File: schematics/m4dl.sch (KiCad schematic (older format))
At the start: 71 parts

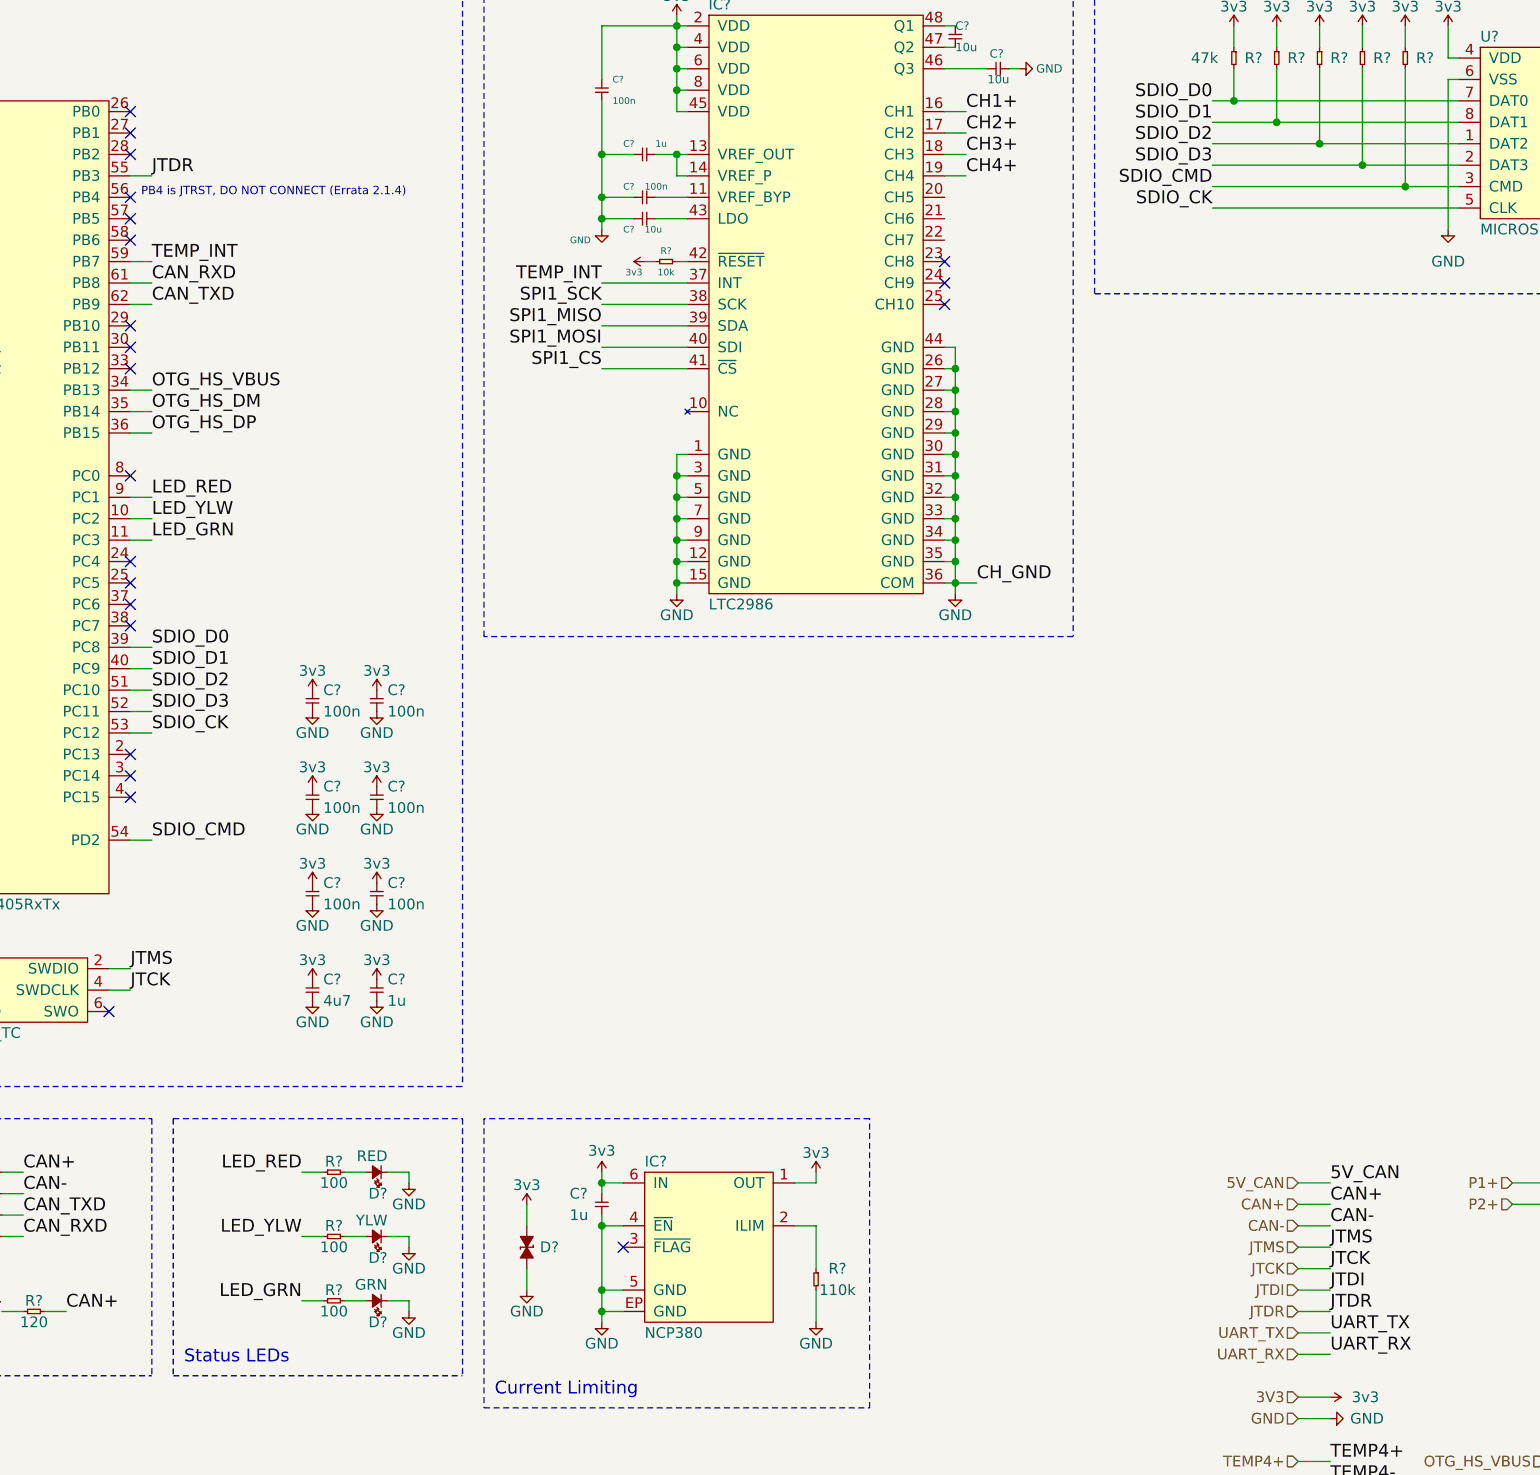
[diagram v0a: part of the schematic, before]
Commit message: Chain JTAG connections
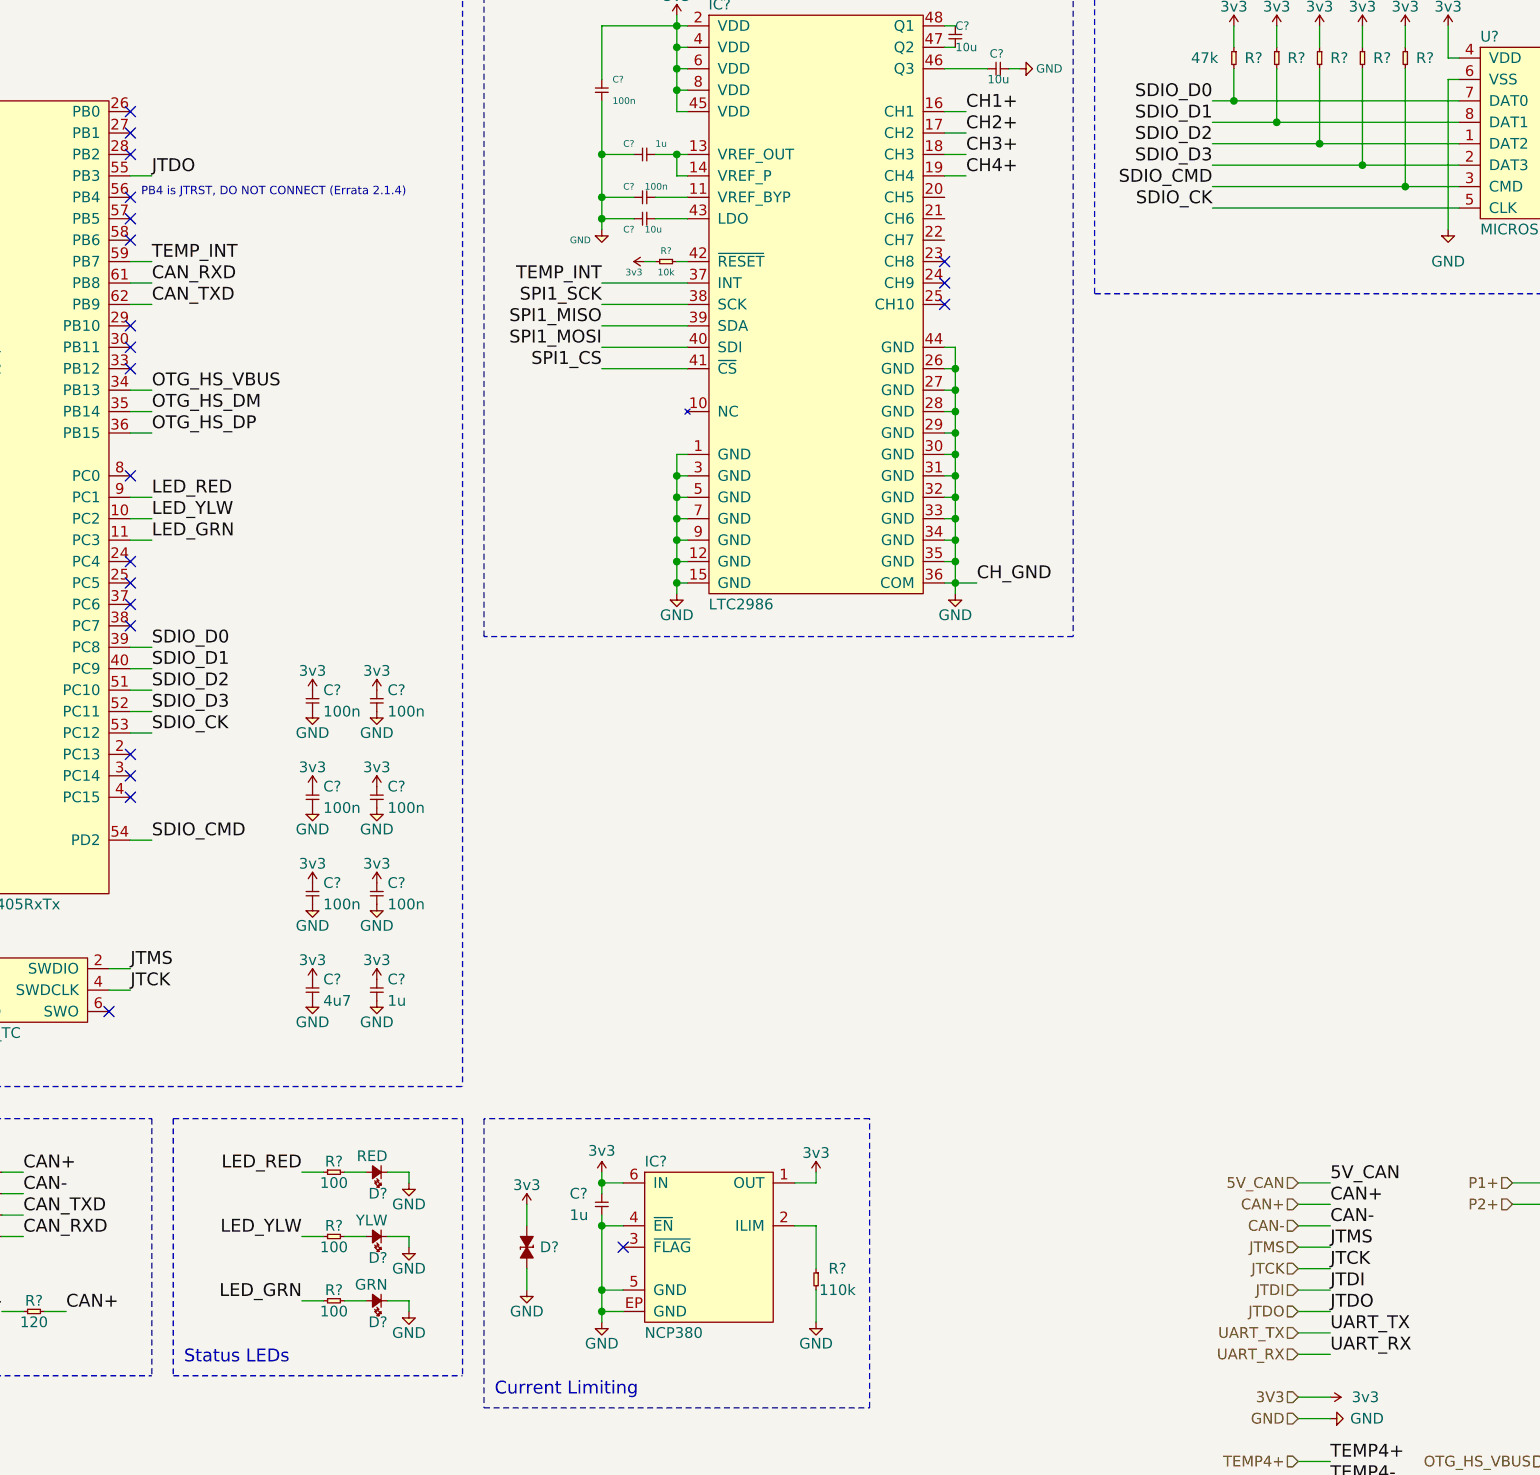
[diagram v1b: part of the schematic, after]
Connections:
- net JTDR renamed JTDO
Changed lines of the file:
@@
 	16050 15100 16050 15150
 Text Label 2950 4300 0    60   ~ 0
-JTDR
+JTDO
 NoConn ~ 2850 4400
 Text Notes 2900 4400 0    39   ~ 0
@@
 Current Limiting
 Text Label 8450 9600 0    60   ~ 0
-JTDR
+JTDO
 Text Label 8450 9700 0    60   ~ 0
 UART_TX
@@
 JTDI
 Text HLabel 8300 9600 0    50   Input ~ 0
-JTDR
+JTDO
 Text Label 8450 10700 0    60   ~ 0
 TEMP2+

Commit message: Master layout reorganisation and cleanup
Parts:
- removed D?: RED, agg:0603-LED, symbol cusf-kicad:LED
- removed D?: YLW, agg:0603-LED, symbol cusf-kicad:LED
- removed D?: GRN, agg:0603-LED, symbol cusf-kicad:LED
- removed IC?: MCP2562, agg:DFN-8-EP-MICROCHIP, symbol cusf-kicad:MCP2562
- removed R?: 120, agg:0603, symbol cusf-kicad:R
- removed R?: 100, agg:0402, symbol cusf-kicad:R
- added D16: RED, agg:0603-LED, symbol cusf-kicad:LED
- added D17: YLW, agg:0603-LED, symbol cusf-kicad:LED
- added D18: GRN, agg:0603-LED, symbol cusf-kicad:LED
- added IC19: MCP2562, agg:DFN-8-EP-MICROCHIP, symbol cusf-kicad:MCP2562
- added R28: 120, agg:0603, symbol cusf-kicad:R
- added R29: 100, agg:0402, symbol cusf-kicad:R
- gave numbers to parts that had none: 65
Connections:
- net 3v3: now also IC19.5 (VIO)
- net 5V_CAN: now also IC19.3 (VDD)
- net CAN+: now also IC19.7 (CANH), R28.2
- net CAN-: now also IC19.6 (CANL), R28.1
- net CAN_RXD: now also IC19.4 (RXD)
- net CAN_TXD: now also IC19.1 (TXD)
- net GND: now also D16.1, D17.1, D18.1, IC19.2 (VSS), IC19.8 (STBY), IC19.EP (VSS)
- net LED_RED: now also R29.1
- net at R31.2: now also D18.2
- net at R30.2: now also D17.2
- new net: D16.2, R29.2

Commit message: Remove pressure UART
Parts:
- removed IC21: ADuM1201, agg:SOIC-8, symbol cusf-kicad:ADuM1201
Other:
- note removed: "PA2 (TX) <-> Pressure 1\nPA3 (RX) <-> Pressure 2"
- note removed: "UART ISOLATOR"
- moved on the sheet: C103, C104, C105, C106, C108, C109, D20, D21, R34, R35, R36, R37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

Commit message: Restructure main schematic bus layout
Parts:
- removed R28: 120, agg:0603, symbol cusf-kicad:R
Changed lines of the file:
@@
 	3050 8700 3050 9900
-Wire Wire Line
-	2550 9600 2450 9600
-Text Label 2550 9600 0    60   ~ 0
-CAN+
-Wire Wire Line
-	2250 9600 2350 9600
-Text Label 2250 9600 2    60   ~ 0
-CAN-
-$Comp
-L cusf-kicad:R R28
-U 1 1 60BFC5F8
-P 2350 9600
-F 0 "R28" H 2400 9650 50  0000 C CNN
-F 1 "120" H 2400 9550 50  0000 C CNN
-F 2 "agg:0603" H 2350 9600 50  0001 C CNN
-F 3 "" H 2350 9600 50  0001 C CNN
-F 4 "9238379" H 2350 9600 60  0001 C CNN "Farnell"
-	1    2350 9600
-	1    0    0    -1
-$EndComp
 Wire Wire Line
 	1400 9350 1400 9400

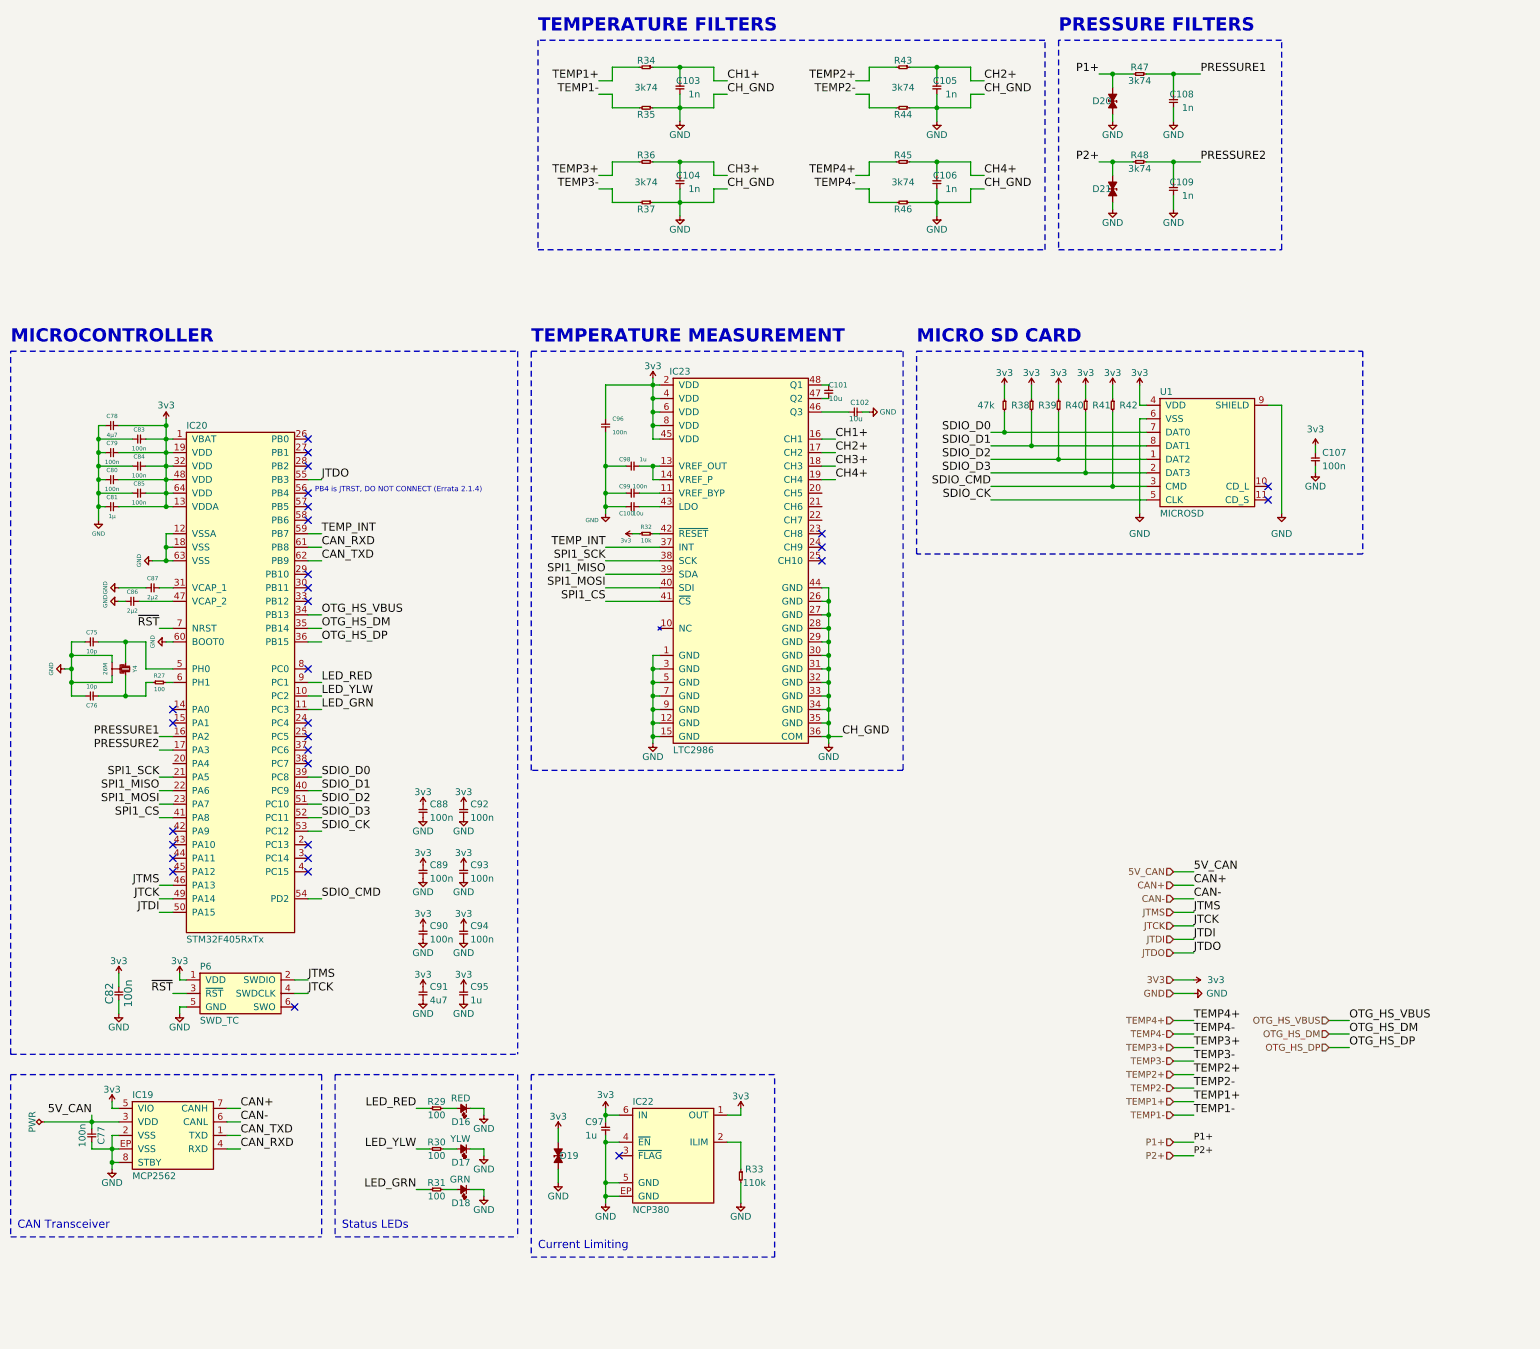
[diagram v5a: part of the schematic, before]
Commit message: Normalise all font sizes to 50 mil
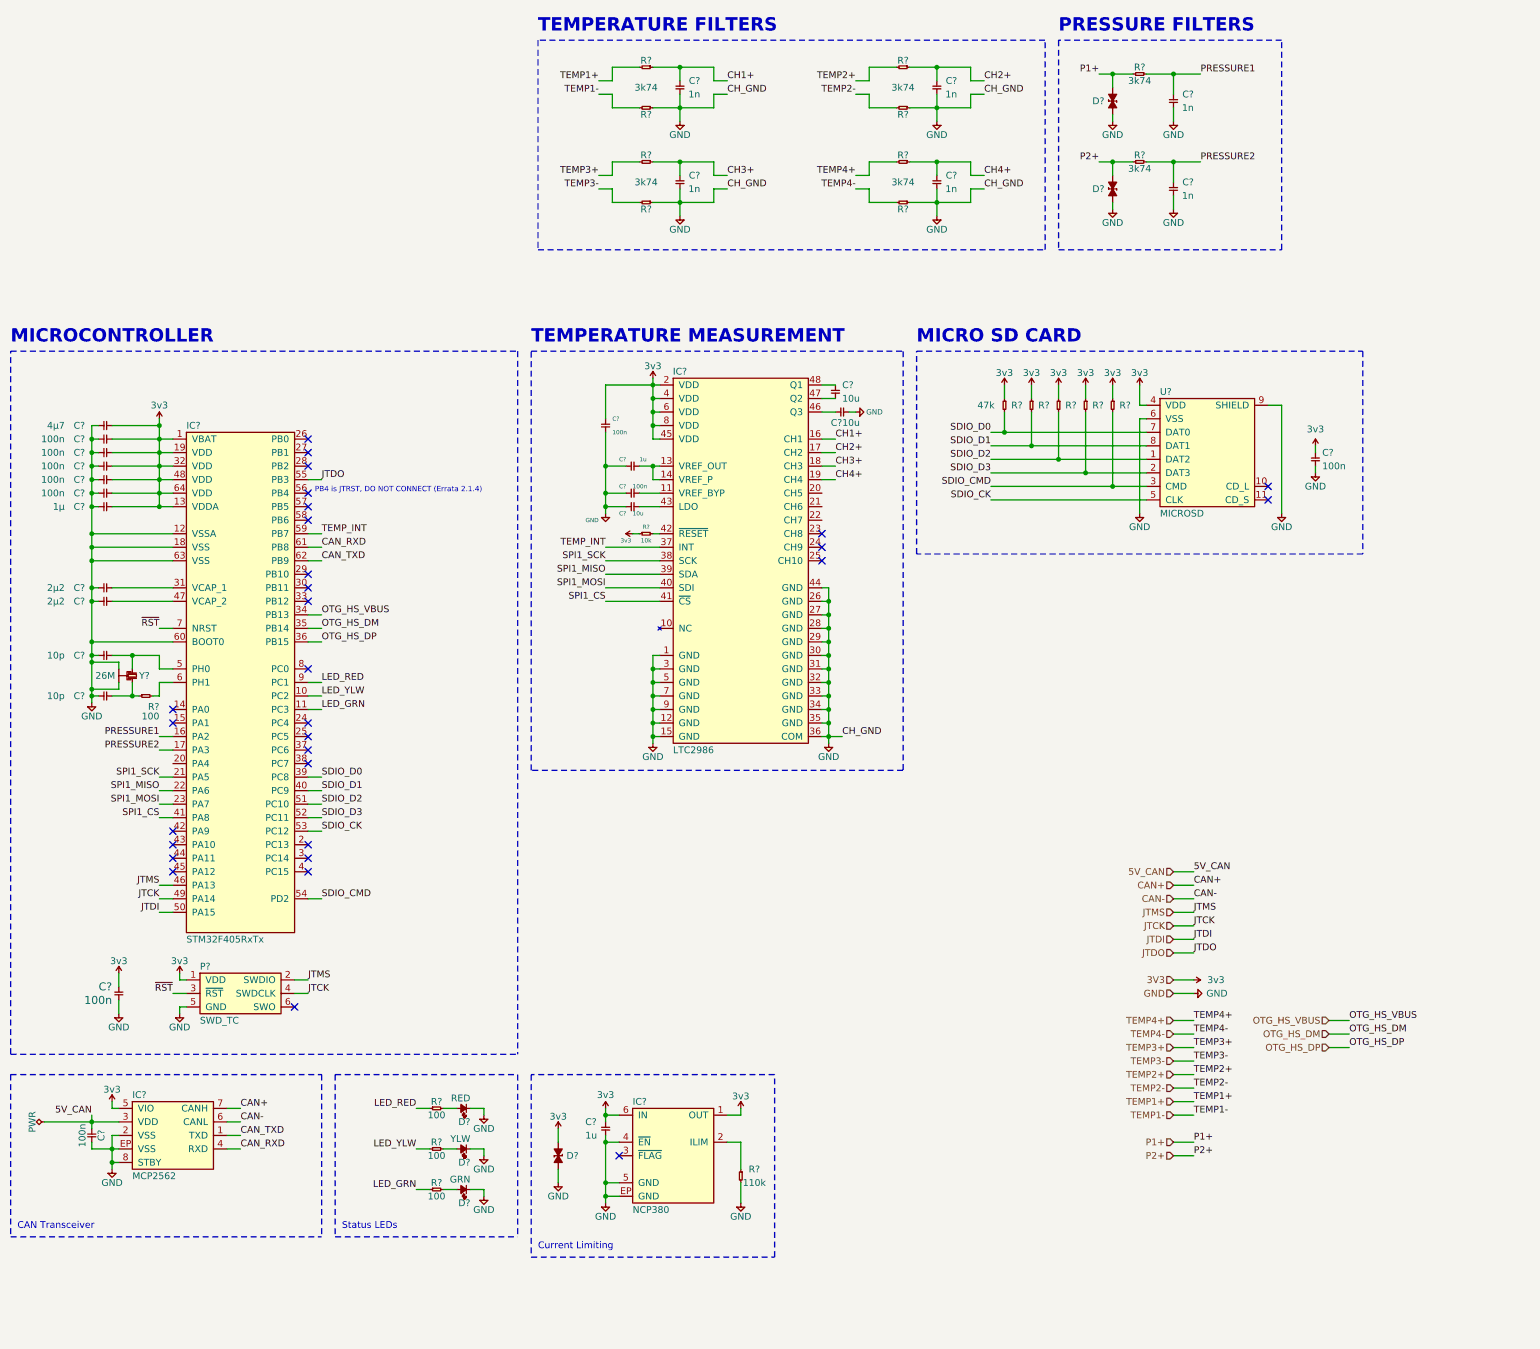
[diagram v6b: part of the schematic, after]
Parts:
- removed C75, C76: 10p, agg:0402, symbol cusf-kicad:C
- removed C78: 4µ7, agg:0402, symbol cusf-kicad:C
- removed C79, C80, C83, C84, C85: 100n, agg:0402, symbol cusf-kicad:C
- removed C81: 1µ, agg:0402, symbol cusf-kicad:C
- removed C86, C87: 2µ2, agg:0402, symbol cusf-kicad:C
- removed C88, C89, C90, C92, C93, C94: 100n, Capacitors_SMD:C_0603, symbol cusf-kicad:C
- removed C91: 4u7, Capacitors_SMD:C_0603, symbol cusf-kicad:C
- removed C95: 1u, Capacitors_SMD:C_0603, symbol cusf-kicad:C
- removed R27: 100, agg:0402, symbol cusf-kicad:R
- removed Y4: 26M, agg:XTAL-20x16, symbol cusf-kicad:SMD_XTAL
- added C? (x2): 2µ2, agg:0402, symbol cusf-kicad:C
- added C? (x5): 100n, agg:0402, symbol cusf-kicad:C
- added C?: 1µ, agg:0402, symbol cusf-kicad:C
- added C?: 4µ7, agg:0402, symbol cusf-kicad:C
- added C? (x2): 10p, agg:0402, symbol cusf-kicad:C
- added R?: 100, agg:0402, symbol cusf-kicad:R
- added Y?: 26M, agg:XTAL-20x16, symbol cusf-kicad:SMD_XTAL
- renumbered C97 to C?, C102 to C?, C77 to C?, C109 to C?, C108 to C?, C82 to C?, C107 to C?, C100 to C?, C106 to C?, C104 to C?, C105 to C?, C103 to C?, C99 to C?, C98 to C?, C96 to C?, C101 to C?, D19 to D?, D21 to D?, D20 to D?, D16 to D?, D17 to D?, D18 to D?, IC20 to IC?, IC22 to IC?, IC23 to IC?, IC19 to IC?, P6 to P?, R31 to R?, R30 to R?, R38 to R?, R39 to R?, R40 to R?, R41 to R?, R42 to R?, R34 to R?, R35 to R?, R36 to R?, R37 to R?, R45 to R?, R46 to R?, R43 to R?, R44 to R?, R47 to R?, R48 to R?, R29 to R?, R32 to R?, R33 to R?, U1 to U?
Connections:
- net 3v3: now also C?.2, C?.2, C?.2, C?.2, C?.2, C?.2, C?.2
- net GND: now also C?.1, C?.1, C?.1, C?.1, C?.1, C?.1, C?.1, C?.1, C?.1, C?.1, C?.1, Y?.2, Y?.4
- net at IC?.31 (VCAP_1): now also C?.2
- net at IC?.47 (VCAP_2): now also C?.2
- net at IC?.5 (PH0): now also C?.2, Y?.1
- net at IC?.6 (PH1): now also R?.2
- new net: C?.2, R?.1, Y?.3
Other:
- moved on the sheet: C?
